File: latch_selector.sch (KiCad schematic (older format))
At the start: 33 parts, among them SW1 SW_DIP_x03, SW3 SW_Push, SW4 Run/Step Mode, U11 74HCT00, U12 74HCT74, U13 MAX6816, U14 LMC555xN, U4 74HCT138, U5 74HCT151, U6 74HCT32

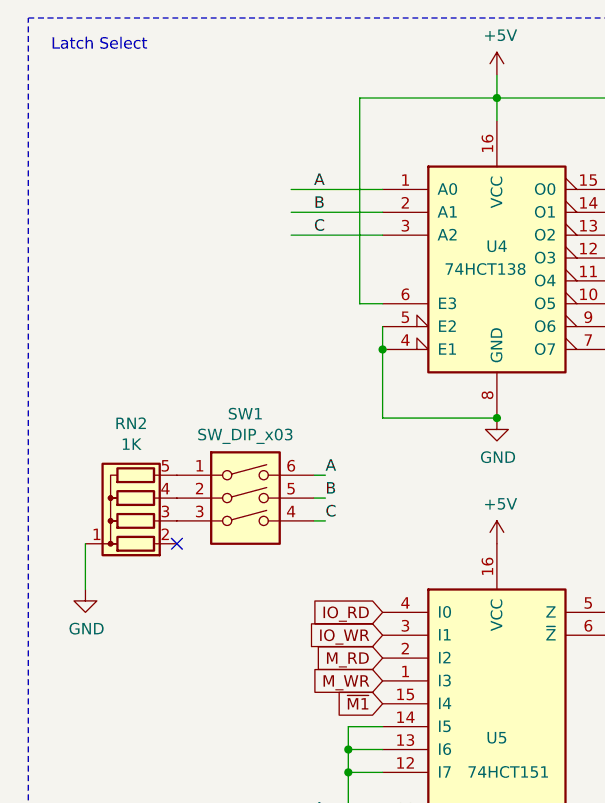
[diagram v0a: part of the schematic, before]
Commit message: added dip sw for latch selection
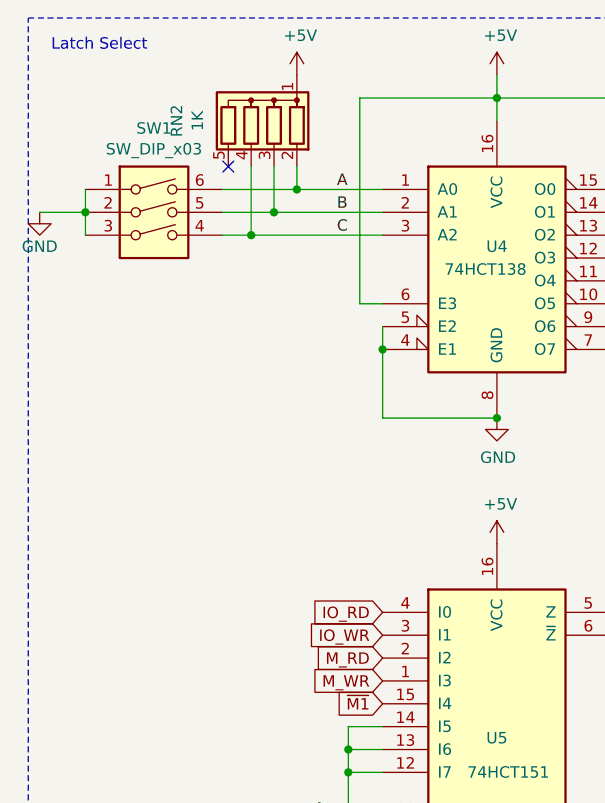
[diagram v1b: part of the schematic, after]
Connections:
- wire segments 118 -> 123
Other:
- moved on the sheet: RN2, SW1
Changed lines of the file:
@@
 EESchema Schematic File Version 5
 LIBS:rc2014_monitor-cache
-EELAYER 30 0
+EELAYER 29 0
 EELAYER END
 $Descr A4 11693 8268
@@
 Wire Wire Line
 	7800 2900 8800 2900
-Connection ~ 2700 2350
-Wire Wire Line
-	2200 2350 2200 2050
-Wire Wire Line
-	2200 1950 2200 2050
-Connection ~ 2200 2050
 Connection ~ 2750 7000
 Wire Wire Line
@@
 F 8 "https://www.mouser.com/ProductDetail/926-LMC555CN-NOPB" H 7300 3400 50  0001 C CNN "SPURL"
 	1    7300 3400
-	1    0    0    -1
-$EndComp
-$Comp
-L rc2014_monitor-rescue:74HCT138-74xx U?
-U 1 1 5CC19E52
-P 2700 1650
-AR Path="/5CC19E52" Ref="U?"  Part="1"
-AR Path="/5CBDBC11/5CC19E52" Ref="U4"  Part="1"
-F 0 "U4" H 2700 1700 50  0000 C CNN
-F 1 "74HCT138" H 2650 1600 50  0000 C CNN
-F 2 "Package_DIP:DIP-16_W7.62mm" H 2700 1650 50  0001 C CNN
-F 3 "http://www.ti.com/lit/ds/symlink/cd74hct138.pdf" H 2700 1650 50  0001 C CNN
-F 4 "Texas Instruments" H -800 -2200 50  0001 C CNN "MFR"
-F 5 "CD74HCT138E" H -800 -2200 50  0001 C CNN "MPN"
-F 6 "Mouser" H -800 -2200 50  0001 C CNN "SPR"
-F 7 "595-CD74HCT138E" H -800 -2200 50  0001 C CNN "SPN"
-F 8 "https://www.mouser.com/ProductDetail/Texas-Instruments/CD74HCT138E?qs=sGAEpiMZZMtxONTBFIcRfpjgwdJpzldARH0rPECqBNk%3D" H -800 -2200 50  0001 C CNN "SPURL"
-	1    2700 1650
 	1    0    0    -1
 $EndComp
@@
 NoConn ~ 7300 4700
 NoConn ~ 7300 4900
-Text Label 1900 1350 0    50   ~ 0
+Text Label 2000 1350 0    50   ~ 0
 A
-Text Label 1900 1450 0    50   ~ 0
+Text Label 2000 1450 0    50   ~ 0
 B
-Text Label 1900 1550 0    50   ~ 0
+Text Label 2000 1550 0    50   ~ 0
 C
-Wire Wire Line
-	1800 1350 2200 1350
-Wire Wire Line
-	1800 1550 2200 1550
-Wire Wire Line
-	1800 1450 2200 1450
 Wire Wire Line
 	1800 4100 2200 4100
@@
 	650  6500 650  600
 Wire Wire Line
-	1900 2600 1950 2600
-Wire Wire Line
-	1900 2700 1950 2700
-Wire Wire Line
-	1900 2800 1950 2800
-Wire Wire Line
-	900  2900 900  3100
-NoConn ~ 1300 2900
+	900  1350 900  1450
+NoConn ~ 1525 1250
+$Comp
+L Switch:SW_DIP_x03 SW1
+U 1 1 5D5736FC
+P 1200 1550
+F 0 "SW1" H 1200 2017 50  0000 C CNN
+F 1 "SW_DIP_x03" H 1200 1926 50  0000 C CNN
+F 2 "Button_Switch_THT:SW_DIP_SPSTx03_Piano_CTS_Series194-3MSTN_W7.62mm_P2.54mm" H 1200 1550 50  0001 C CNN
+F 3 "~" H 1200 1550 50  0001 C CNN
+	1    1200 1550
+	1    0    0    -1
+$EndComp
+$Comp
+L Device:R_Network04 RN2
+U 1 1 5D5736FD
+P 1625 1050
+F 0 "RN2" V 1950 1050 50  0000 C CNN
+F 1 "1K" V 1859 1050 50  0000 C CNN
+F 2 "Resistor_THT:R_Array_SIP5" V 1900 1050 50  0001 C CNN
+F 3 "http://www.vishay.com/docs/31509/csc.pdf" H 1625 1050 50  0001 C CNN
+	1    1625 1050
+	-1   0    0    -1
+$EndComp
+Connection ~ 2700 2350
+Wire Wire Line
+	2200 1950 2200 2050
+Wire Wire Line
+	2200 2350 2200 2050
+Connection ~ 2200 2050
+$Comp
+L rc2014_monitor-rescue:74HCT138-74xx U?
+U 1 1 5CC19E52
+P 2700 1650
+AR Path="/5CC19E52" Ref="U?"  Part="1"
+AR Path="/5CBDBC11/5CC19E52" Ref="U4"  Part="1"
+F 0 "U4" H 2700 1700 50  0000 C CNN
+F 1 "74HCT138" H 2650 1600 50  0000 C CNN
+F 2 "Package_DIP:DIP-16_W7.62mm" H 2700 1650 50  0001 C CNN
+F 3 "http://www.ti.com/lit/ds/symlink/cd74hct138.pdf" H 2700 1650 50  0001 C CNN
+F 4 "Texas Instruments" H -800 -2200 50  0001 C CNN "MFR"
+F 5 "CD74HCT138E" H -800 -2200 50  0001 C CNN "MPN"
+F 6 "Mouser" H -800 -2200 50  0001 C CNN "SPR"
+F 7 "595-CD74HCT138E" H -800 -2200 50  0001 C CNN "SPN"
+F 8 "https://www.mouser.com/ProductDetail/Texas-Instruments/CD74HCT138E?qs=sGAEpiMZZMtxONTBFIcRfpjgwdJpzldARH0rPECqBNk%3D" H -800 -2200 50  0001 C CNN "SPURL"
+	1    2700 1650
+	1    0    0    -1
+$EndComp
+Wire Wire Line
+	2200 1450 1725 1450
+Wire Wire Line
+	2200 1350 1825 1350
+Wire Wire Line
+	1625 1250 1625 1550
+Wire Wire Line
+	1725 1250 1725 1450
+Wire Wire Line
+	1825 1250 1825 1350
+Connection ~ 900  1450
+Wire Wire Line
+	900  1450 900  1550
+Wire Wire Line
+	900  1450 700  1450
+$Comp
+L power:+5V #PWR?
+U 1 1 5D42948B
+P 1825 850
+AR Path="/5D42948B" Ref="#PWR?"  Part="1"
+AR Path="/5CB63856/5D42948B" Ref="#PWR?"  Part="1"
+AR Path="/5CB5AB00/5CB63856/5D42948B" Ref="#PWR?"  Part="1"
+AR Path="/5CBDBC11/5D42948B" Ref="#PWR?"  Part="1"
+F 0 "#PWR?" H 1825 700 50  0001 C CNN
+F 1 "+5V" H 1840 1023 50  0000 C CNN
+F 2 "" H 1825 850 50  0001 C CNN
+F 3 "" H 1825 850 50  0001 C CNN
+	1    1825 850
+	1    0    0    -1
+$EndComp
 $Comp
 L power:GND #PWR?
 U 1 1 5D5736FB
-P 900 3100
+P 700 1450
 AR Path="/5D5736FB" Ref="#PWR?"  Part="1"
 AR Path="/5CB63856/5D5736FB" Ref="#PWR?"  Part="1"
 AR Path="/5CB5AB00/5CB63856/5D5736FB" Ref="#PWR?"  Part="1"
 AR Path="/5CBDBC11/5D5736FB" Ref="#PWR01"  Part="1"
-F 0 "#PWR01" H 900 2850 50  0001 C CNN
-F 1 "GND" H 905 2927 50  0000 C CNN
-F 2 "" H 900 3100 50  0001 C CNN
-F 3 "" H 900 3100 50  0001 C CNN
-	1    900  3100
-	1    0    0    -1
-$EndComp
-Text Label 1950 2700 0    50   ~ 0
-B
-Text Label 1950 2800 0    50   ~ 0
-C
-$Comp
-L Switch:SW_DIP_x03 SW1
-U 1 1 5D5736FC
-P 1600 2800
-F 0 "SW1" H 1600 3267 50  0000 C CNN
-F 1 "SW_DIP_x03" H 1600 3176 50  0000 C CNN
-F 2 "Button_Switch_THT:SW_DIP_SPSTx03_Piano_CTS_Series194-3MSTN_W7.62mm_P2.54mm" H 1600 2800 50  0001 C CNN
-F 3 "~" H 1600 2800 50  0001 C CNN
-	1    1600 2800
-	1    0    0    -1
-$EndComp
-$Comp
-L Device:R_Network04 RN2
-U 1 1 5D5736FD
-P 1100 2700
-F 0 "RN2" V 1425 2700 50  0000 C CNN
-F 1 "1K" V 1334 2700 50  0000 C CNN
-F 2 "Resistor_THT:R_Array_SIP5" V 1375 2700 50  0001 C CNN
-F 3 "http://www.vishay.com/docs/31509/csc.pdf" H 1100 2700 50  0001 C CNN
-	1    1100 2700
-	0    -1   -1   0
-$EndComp
-Text Label 1950 2600 0    50   ~ 0
-A
+F 0 "#PWR01" H 700 1200 50  0001 C CNN
+F 1 "GND" H 700 1300 50  0000 C CNN
+F 2 "" H 700 1450 50  0001 C CNN
+F 3 "" H 700 1450 50  0001 C CNN
+	1    700  1450
+	-1   0    0    -1
+$EndComp
+Connection ~ 1625 1550
+Wire Wire Line
+	1625 1550 1500 1550
+Connection ~ 1725 1450
+Connection ~ 1825 1350
+Wire Wire Line
+	1625 1550 2200 1550
+Wire Wire Line
+	1500 1350 1825 1350
+Wire Wire Line
+	1500 1450 1725 1450
 $EndSCHEMATC

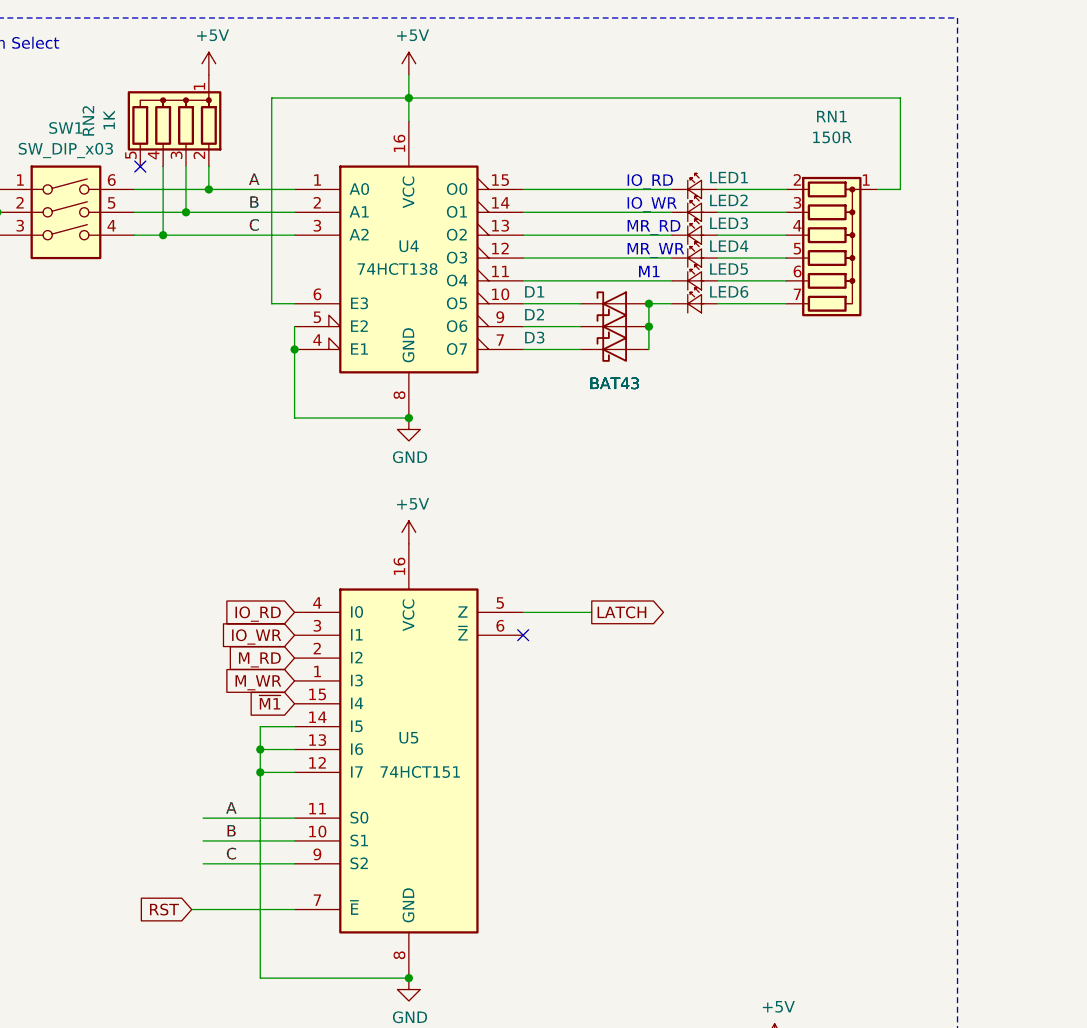
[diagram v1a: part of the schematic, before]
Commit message: tightened up gnd plane and schematics
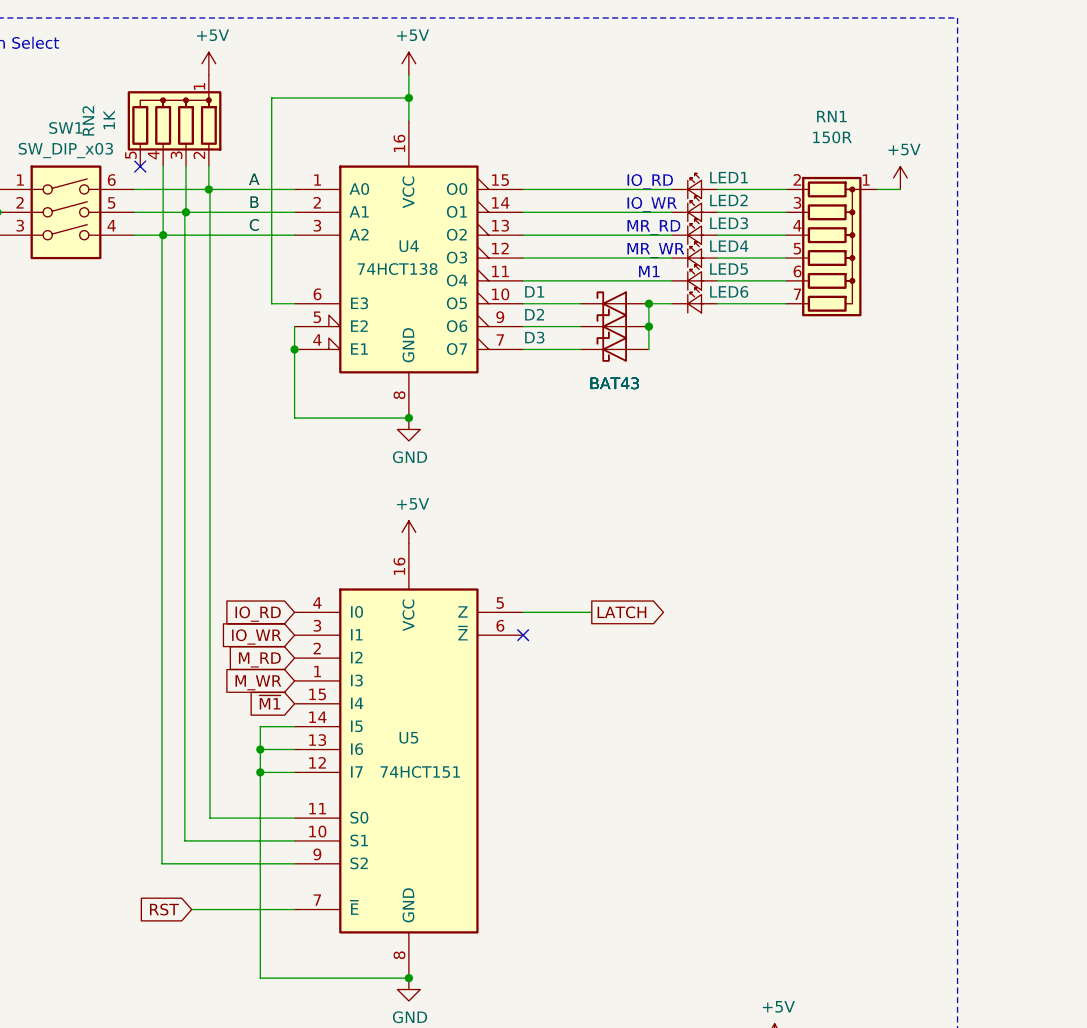
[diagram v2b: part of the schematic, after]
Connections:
- net A: no longer U5.11 (S0)
- net B: no longer U5.10 (S1)
- net C: no longer U5.9 (S2)
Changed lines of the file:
@@
 EESchema Schematic File Version 5
 LIBS:rc2014_monitor-cache
-EELAYER 29 0
+EELAYER 30 0
 EELAYER END
 $Descr A4 11693 8268
@@
 	2750 6850 2750 7000
 Wire Wire Line
-	4850 950  4850 1350
-Wire Wire Line
 	4050 1350 4350 1350
 Wire Wire Line
@@
 Wire Wire Line
 	3200 1350 3850 1350
-Wire Wire Line
-	2700 950  4850 950
 Wire Wire Line
 	3200 1750 3850 1750
@@
 Text Label 2000 1550 0    50   ~ 0
 C
-Wire Wire Line
-	1800 4100 2200 4100
-Wire Wire Line
-	1800 4200 2200 4200
-Wire Wire Line
-	1800 4300 2200 4300
-Text Label 1900 4100 0    50   ~ 0
-A
-Text Label 1900 4200 0    50   ~ 0
-B
-Text Label 1900 4300 0    50   ~ 0
-C
 Wire Notes Line
 	650  6500 650  600
@@
 Wire Wire Line
 	1500 1450 1725 1450
+$Comp
+L power:+5V #PWR?
+U 1 1 5D44220F
+P 4850 1350
+AR Path="/5D44220F" Ref="#PWR?"  Part="1"
+AR Path="/5CB63856/5D44220F" Ref="#PWR?"  Part="1"
+AR Path="/5CB5AB00/5CB63856/5D44220F" Ref="#PWR?"  Part="1"
+AR Path="/5CBDBC11/5D44220F" Ref="#PWR?"  Part="1"
+F 0 "#PWR?" H 4850 1200 50  0001 C CNN
+F 1 "+5V" H 4865 1523 50  0000 C CNN
+F 2 "" H 4850 1350 50  0001 C CNN
+F 3 "" H 4850 1350 50  0001 C CNN
+	1    4850 1350
+	1    0    0    -1
+$EndComp
+Wire Wire Line
+	2200 4100 1830 4100
+Wire Wire Line
+	1830 4100 1830 1350
+Wire Wire Line
+	2200 4200 1720 4200
+Wire Wire Line
+	1720 4200 1720 1450
+Wire Wire Line
+	2200 4300 1620 4300
+Wire Wire Line
+	1620 4300 1620 1550
 $EndSCHEMATC

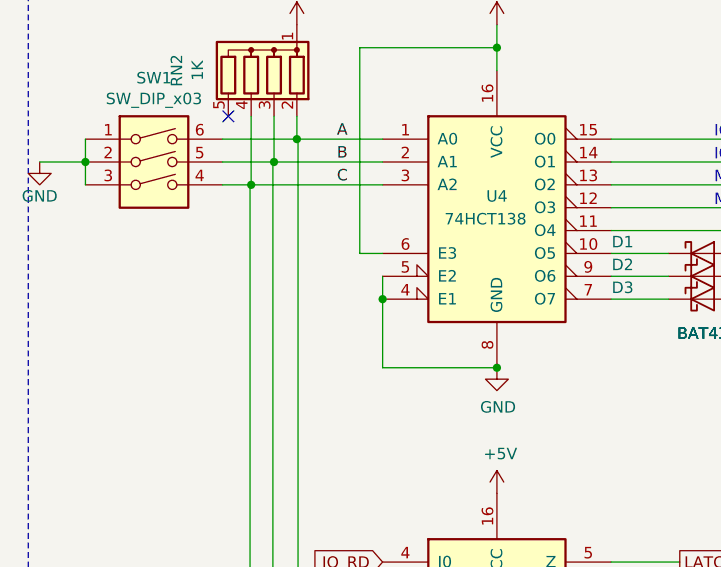
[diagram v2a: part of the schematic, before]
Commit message: extended active high reset to displays and ics
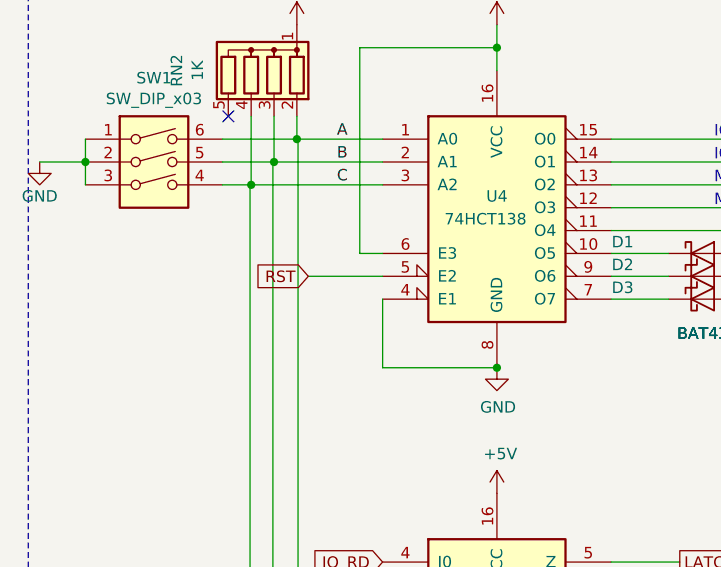
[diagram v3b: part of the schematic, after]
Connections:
- net GND: no longer U4.5 (E2)
- net RST: now also U4.5 (E2)
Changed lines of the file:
@@
 Connection ~ 2700 2350
 Wire Wire Line
-	2200 1950 2200 2050
-Wire Wire Line
 	2200 2350 2200 2050
-Connection ~ 2200 2050
 $Comp
 L rc2014_monitor-rescue:74HCT138-74xx U?
@@
 Wire Wire Line
 	1620 4300 1620 1550
+Wire Wire Line
+	2200 1950 1875 1950
+Text GLabel 1875 1950 0    50   Input ~ 0
+RST
 $EndSCHEMATC

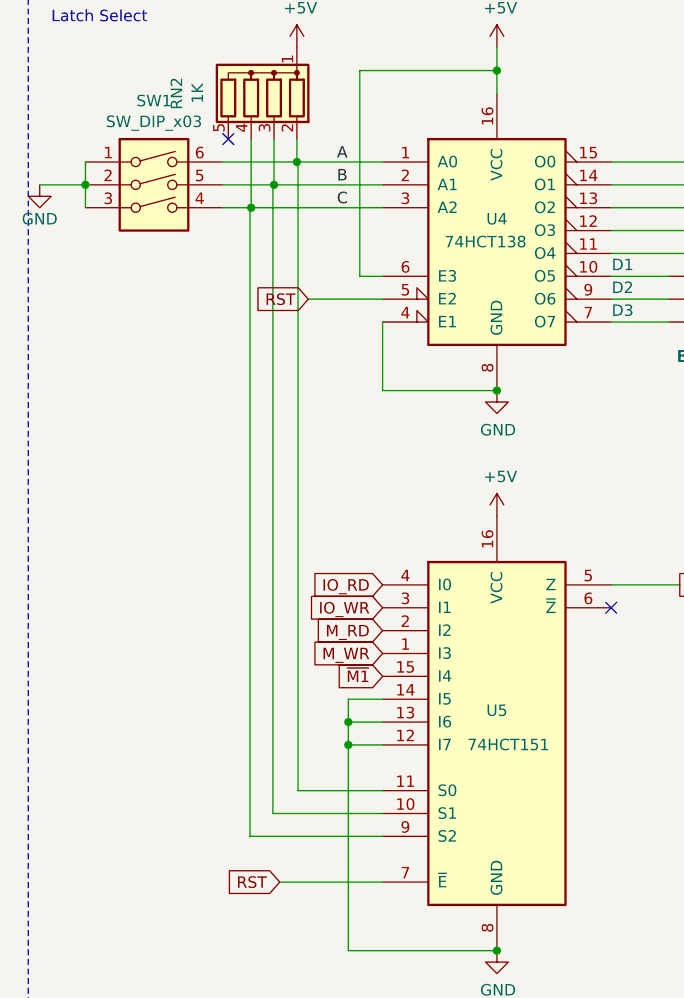
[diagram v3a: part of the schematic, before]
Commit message: fixed via sizes and silk
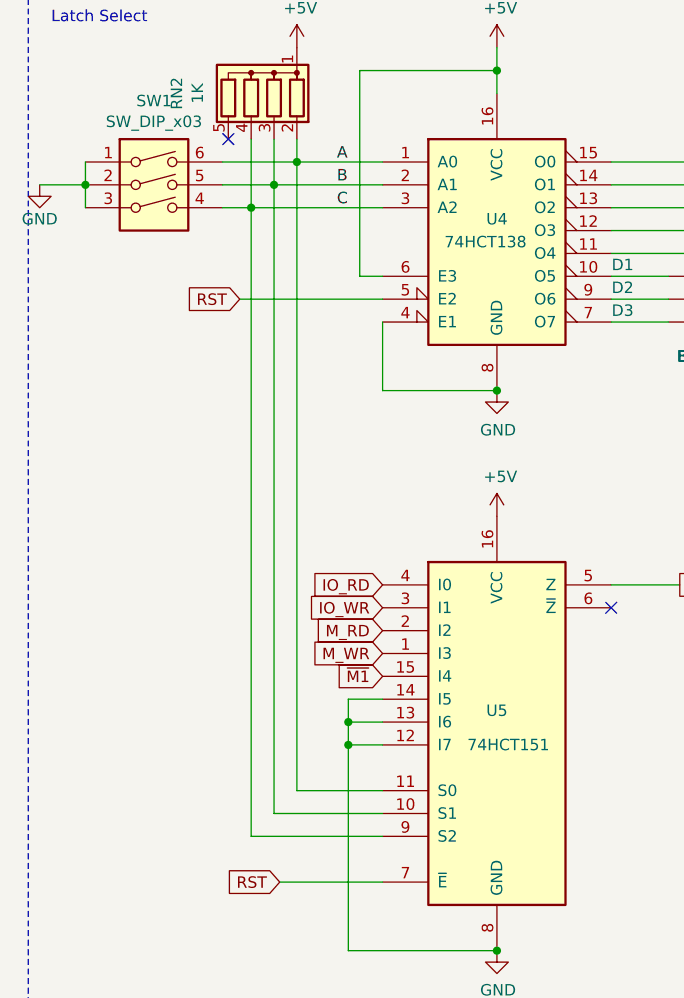
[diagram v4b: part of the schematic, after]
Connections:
- net A: now also U5.11 (S0)
- net B: now also U5.10 (S1)
- net C: now also U5.9 (S2)
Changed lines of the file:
@@
 AR Path="/5CB63856/5D42948B" Ref="#PWR?"  Part="1"
 AR Path="/5CB5AB00/5CB63856/5D42948B" Ref="#PWR?"  Part="1"
-AR Path="/5CBDBC11/5D42948B" Ref="#PWR?"  Part="1"
-F 0 "#PWR?" H 1825 700 50  0001 C CNN
+AR Path="/5CBDBC11/5D42948B" Ref="#PWR0119"  Part="1"
+F 0 "#PWR0119" H 1825 700 50  0001 C CNN
 F 1 "+5V" H 1840 1023 50  0000 C CNN
 F 2 "" H 1825 850 50  0001 C CNN
@@
 AR Path="/5CB63856/5D44220F" Ref="#PWR?"  Part="1"
 AR Path="/5CB5AB00/5CB63856/5D44220F" Ref="#PWR?"  Part="1"
-AR Path="/5CBDBC11/5D44220F" Ref="#PWR?"  Part="1"
-F 0 "#PWR?" H 4850 1200 50  0001 C CNN
+AR Path="/5CBDBC11/5D44220F" Ref="#PWR0135"  Part="1"
+F 0 "#PWR0135" H 4850 1200 50  0001 C CNN
 F 1 "+5V" H 4865 1523 50  0000 C CNN
 F 2 "" H 4850 1350 50  0001 C CNN
@@
 $EndComp
 Wire Wire Line
-	2200 4100 1830 4100
+	2200 1950 1575 1950
+Text GLabel 1575 1950 0    50   Input ~ 0
+RST
 Wire Wire Line
-	1830 4100 1830 1350
+	2200 4100 1825 4100
 Wire Wire Line
-	2200 4200 1720 4200
+	1825 4100 1825 1350
 Wire Wire Line
-	1720 4200 1720 1450
+	2200 4200 1725 4200
 Wire Wire Line
-	2200 4300 1620 4300
+	1725 4200 1725 1450
 Wire Wire Line
-	1620 4300 1620 1550
+	2200 4300 1625 4300
 Wire Wire Line
-	2200 1950 1875 1950
-Text GLabel 1875 1950 0    50   Input ~ 0
-RST
+	1625 4300 1625 1550
 $EndSCHEMATC
